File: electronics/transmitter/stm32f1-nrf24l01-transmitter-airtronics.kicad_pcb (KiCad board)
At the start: 2 copper layers, 107 x 36 mm, 31 parts, among them K1 CONN_3, K10 CONN_3, K11 CONN_3, K12 UART, K2 CONN_3, K3 CONN_3, K4 CONN_3, K5 CONN_3, K6 CONN_3, K7 CONN_3, K8 CONN_3, K9 CONN_3, P1 Charge, P2 LED, P3 PWR-BAT, P4 PWR-IN, P5 Buzzer, Q1 BC547B, SW1 ON/OFF, U1 LIPO_CHARGER_+_PROTECTION, U2 STM32F103C8T6_DEV_BOARD, U3 NRF24L01P

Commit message: Tweak layout
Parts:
- removed SP1: SPEAKER, WLA:Buzzer_passive
- added P1: Charge, Pin_Headers:Pin_Header_Straight_1x02_Pitch2.54mm, F.Cu at (276.9, 111.8)
- added REF**: MountingHole_3.2mm_M3, Mounting_Holes:MountingHole_3.2mm_M3, F.Cu at (210.8, 111.8)
- moved K12 15.2 mm to (241.3, 160.0)
- moved K10 13.7 mm to (221.0, 88.9)
- moved K8 13.7 mm to (228.6, 88.9)
- moved K11 13.7 mm to (223.5, 88.9)
- moved K9 13.7 mm to (226.1, 88.9)
- moved P3 12.7 mm to (276.9, 157.5)
- moved P4 12.7 mm to (269.2, 157.5)
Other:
- board size 107 x 36 mm -> 91.4 x 33 mm
- board text added: "+5V in charge/Red LED"
- board text added: "+After switch/+Buzzer"
- board text added: "+Batt protected"
- board text added: "-Red LED"
- board text added: "CH3"
- board text added: "DR-pot"
- board text added: "DR-switch"
- board text added: "ST"
- board text added: "ST-trim"
- board text added: "TH"
- board text added: "TH-trim"
- board text removed: "+5V in charge"
- board text removed: "+Switched/Buzzer"
- board text removed: "+batt protected"
- board text removed: "40"

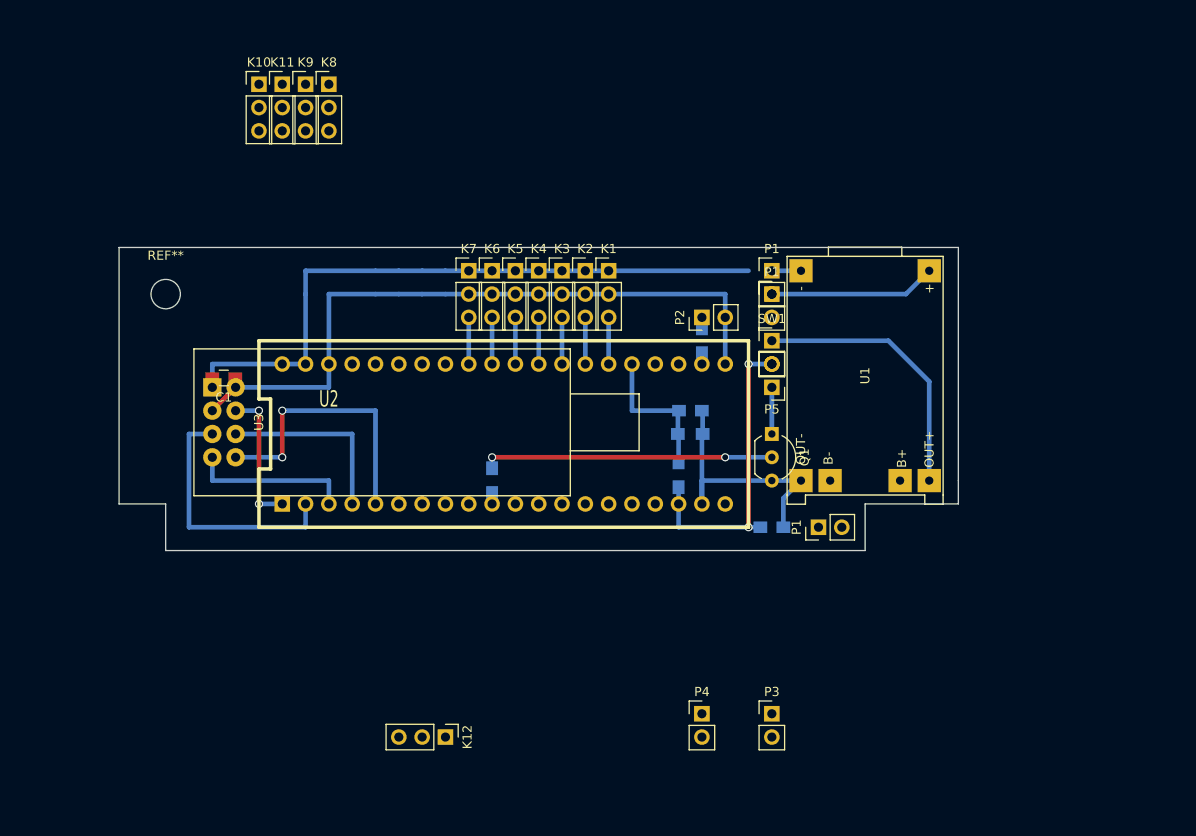
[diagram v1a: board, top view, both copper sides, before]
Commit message: Make PCB smaller and annotate
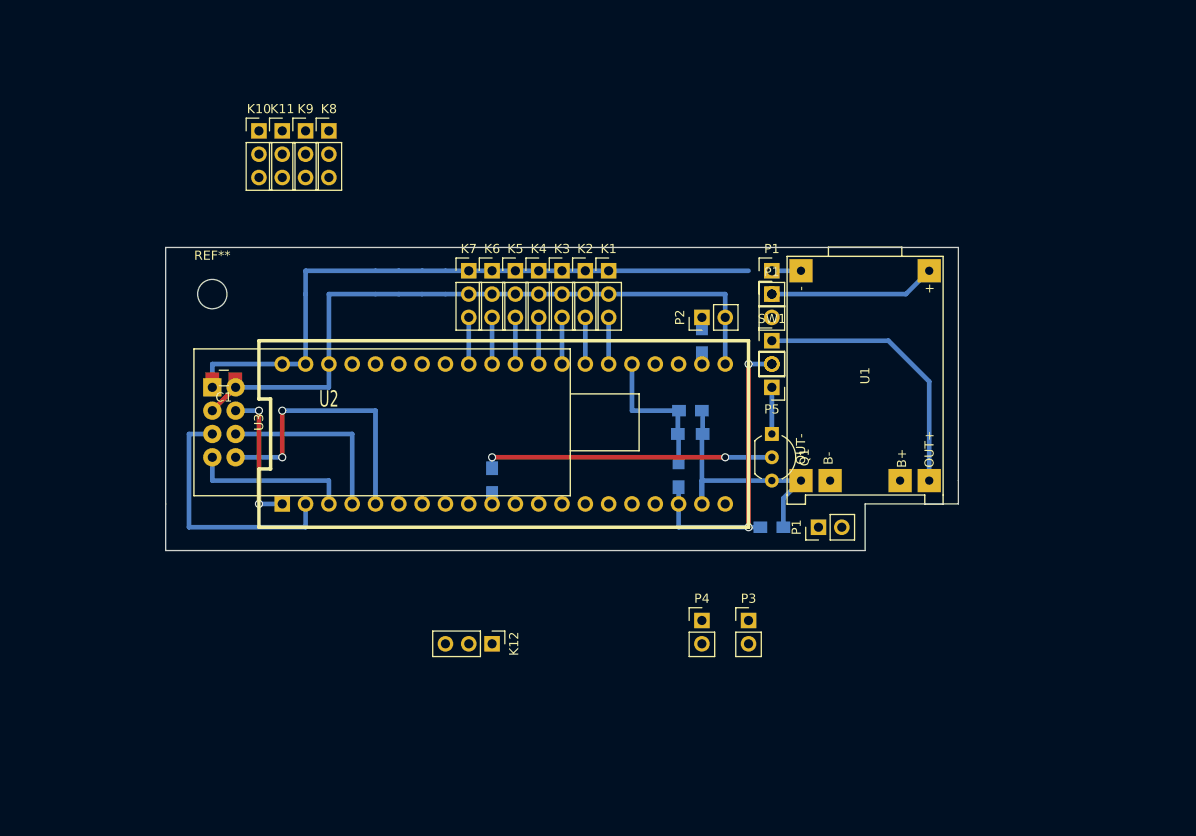
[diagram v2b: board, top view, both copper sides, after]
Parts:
- moved K12 11.4 mm to (246.4, 149.9)
- moved P3 10.5 mm to (274.3, 147.3)
- moved P4 10.2 mm to (269.2, 147.3)
- moved REF** 5.08 mm to (215.9, 111.8)
- moved K10 5.08 mm to (221.0, 94.0)
- moved K11 5.08 mm to (223.5, 94.0)
- moved K8 5.08 mm to (228.6, 94.0)
- moved K9 5.08 mm to (226.1, 94.0)
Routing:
- net Net-(P1-Pad2): track 18.8 -> 4.23 mm
- net Net-(P1-Pad1): track 3.18 -> 17.8 mm
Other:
- board size 91.4 x 33 mm -> 86.4 x 33 mm
- board text added: "34"
- board text added: "Links: 4, 2, 10, 7"
- board text removed: "35"

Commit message: Add annotations
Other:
- board text added: "This is not a PCB, but meant to be build on a prototyping PCB. It fits in the battery area of the Airtronics car transmitter. Modifications needed: STM32: remove BOOT pin header and tie to ground STM32: change programming pin header to vertical style TP4056: Change charge resistor to 2k7 (440mA) TP4056: Remove tabs near batt pads TP4056: Remove red LED, connect to pin header "-Red LED" nRF24L01+ 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"
- board text added: "Wire links needed: 4, 2, 10, 7"
- board text removed: "Links: 4, 2, 10, 7"
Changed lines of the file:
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@@
     (links 78)
     (no_connects 29)
-    (area 206.441257 89.742856 332.228571 153.2266)
+    (area 206.441257 89.742856 387.919999 165.235)
     (thickness 1.6)
-    (drawings 50)
+    (drawings 51)
     (tracks 102)
     (zones 0)
@@
     (41 Cmts.User user)
     (42 Eco1.User user hide)
-    (43 Eco2.User user hide)
+    (43 Eco2.User user)
     (44 Edge.Cuts user)
   )
@@
     (aux_axis_origin 210.82 139.7)
     (grid_origin 210.82 139.7)
-    (visible_elements 7FFCD71F)
+    (visible_elements 7FFCCF1F)
     (pcbplotparams
       (layerselection 0x00030_80000001)
@@
     (pad 1 np_thru_hole circle (at 0 0) (size 3.2 3.2) (drill 3.2) (layers *.Cu *.Mask))
   )
-  (gr_text "Links: 4, 2, 10, 7" (at 220.98 149.86) (layer Cmts.User)
-    (effects (font (size 2.032 2.032) (thickness 0.3)))
+  (gr_text "This is not a PCB, but meant to be build on a prototyping PCB.\nIt fits in the battery area of the Airtronics car transmitter.\n\nModifications needed:\nSTM32: remove BOOT pin header and tie to ground\nSTM32: change programming pin header to vertical style\nTP4056: Change charge resistor to 2k7 (440mA)\nTP4056: Remove tabs near batt pads\nTP4056: Remove red LED, connect to pin header \"-Red LED\"\nnRF24L01+ PA: Remove antenna socket and use antenna on wire\nnRF24L01+ PA: Longer pin headers\nnRF24L01+ PA: Connect CE to Vcc\nnRF24L01+ PA: Large cap between Vcc and GND" (at 312.42 149.86) (layer Eco2.User)
+    (effects (font (size 1.5 1.5) (thickness 0.3)) (justify left))
+  )
+  (gr_text "Wire links needed: 4, 2, 10, 7" (at 228.6 157.48) (layer Eco2.User)
+    (effects (font (thickness 0.3)))
   )
   (gr_line (start 210.82 106.68) (end 297.18 106.68) (angle 90) (layer Edge.Cuts) (width 0.1))
   (gr_line (start 210.82 134.62) (end 210.82 106.68) (angle 90) (layer Edge.Cuts) (width 0.1))
-  (gr_text DR-switch (at 243.84 101.6 90) (layer Cmts.User)
-    (effects (font (size 1.5 1.5) (thickness 0.3)) (justify left))
-  )
-  (gr_text DR-pot (at 246.38 101.6 90) (layer Cmts.User)
-    (effects (font (size 1.5 1.5) (thickness 0.3)) (justify left))
-  )
-  (gr_text TH (at 248.92 101.6 90) (layer Cmts.User)
-    (effects (font (size 1.5 1.5) (thickness 0.3)) (justify left))
-  )
-  (gr_text TH-trim (at 251.46 101.6 90) (layer Cmts.User)
-    (effects (font (size 1.5 1.5) (thickness 0.3)) (justify left))
-  )
-  (gr_text CH3 (at 254 101.6 90) (layer Cmts.User)
-    (effects (font (size 1.5 1.5) (thickness 0.3)) (justify left))
-  )
-  (gr_text ST-trim (at 256.54 101.6 90) (layer Cmts.User)
-    (effects (font (size 1.5 1.5) (thickness 0.3)) (justify left))
-  )
-  (gr_text ST (at 259.08 101.6 90) (layer Cmts.User)
+  (gr_text DR-switch (at 243.84 101.6 90) (layer Eco2.User)
+    (effects (font (size 1.5 1.5) (thickness 0.3)) (justify left))
+  )
+  (gr_text DR-pot (at 246.38 101.6 90) (layer Eco2.User)
+    (effects (font (size 1.5 1.5) (thickness 0.3)) (justify left))
+  )
+  (gr_text TH (at 248.92 101.6 90) (layer Eco2.User)
+    (effects (font (size 1.5 1.5) (thickness 0.3)) (justify left))
+  )
+  (gr_text TH-trim (at 251.46 101.6 90) (layer Eco2.User)
+    (effects (font (size 1.5 1.5) (thickness 0.3)) (justify left))
+  )
+  (gr_text CH3 (at 254 101.6 90) (layer Eco2.User)
+    (effects (font (size 1.5 1.5) (thickness 0.3)) (justify left))
+  )
+  (gr_text ST-trim (at 256.54 101.6 90) (layer Eco2.User)
+    (effects (font (size 1.5 1.5) (thickness 0.3)) (justify left))
+  )
+  (gr_text ST (at 259.08 101.6 90) (layer Eco2.User)
     (effects (font (size 1.5 1.5) (thickness 0.3)) (justify left))
   )
@@
   (gr_line (start 297.18 106.68) (end 297.18 132.08) (angle 90) (layer Edge.Cuts) (width 0.1))
   (gr_line (start 210.82 139.7) (end 210.82 134.62) (angle 90) (layer Edge.Cuts) (width 0.1))
-  (gr_text "-Red LED" (at 304.8 114.3) (layer Cmts.User)
-    (effects (font (size 1.5 1.5) (thickness 0.3)) (justify left))
-  )
-  (gr_text Meter- (at 269.24 101.6 90) (layer Cmts.User)
-    (effects (font (size 1.5 1.5) (thickness 0.3)) (justify left))
-  )
-  (gr_text Meter+ (at 271.78 101.6 90) (layer Cmts.User)
-    (effects (font (size 1.5 1.5) (thickness 0.3)) (justify left))
-  )
-  (gr_text Batt+ (at 284.48 144.78 90) (layer Cmts.User)
+  (gr_text "-Red LED" (at 304.8 114.3) (layer Eco2.User)
+    (effects (font (size 1.5 1.5) (thickness 0.3)) (justify left))
+  )
+  (gr_text Meter- (at 269.24 101.6 90) (layer Eco2.User)
+    (effects (font (size 1.5 1.5) (thickness 0.3)) (justify left))
+  )
+  (gr_text Meter+ (at 271.78 101.6 90) (layer Eco2.User)
+    (effects (font (size 1.5 1.5) (thickness 0.3)) (justify left))
+  )
+  (gr_text Batt+ (at 284.48 144.78 90) (layer Eco2.User)
     (effects (font (size 1.5 1.5) (thickness 0.3)) (justify right))
   )
-  (gr_text Batt- (at 281.94 144.78 90) (layer Cmts.User)
+  (gr_text Batt- (at 281.94 144.78 90) (layer Eco2.User)
     (effects (font (size 1.5 1.5) (thickness 0.3)) (justify right))
   )
-  (gr_text GND (at 304.8 109.22) (layer Cmts.User)
-    (effects (font (size 1.5 1.5) (thickness 0.3)) (justify left))
-  )
-  (gr_text "+5V in charge/Red LED" (at 304.8 111.76) (layer Cmts.User)
-    (effects (font (size 1.5 1.5) (thickness 0.3)) (justify left))
-  )
-  (gr_text "+Batt protected" (at 304.8 116.84) (layer Cmts.User)
-    (effects (font (size 1.5 1.5) (thickness 0.3)) (justify left))
-  )
-  (gr_text "+After switch/+Buzzer" (at 304.8 119.38) (layer Cmts.User)
-    (effects (font (size 1.5 1.5) (thickness 0.3)) (justify left))
-  )
-  (gr_text -Buzzer (at 304.8 121.92) (layer Cmts.User)
-    (effects (font (size 1.5 1.5) (thickness 0.3)) (justify left))
-  )
+  (gr_text GND (at 304.8 109.22) (layer Eco2.User)
+    (effects (font (size 1.5 1.5) (thickness 0.3)) (justify left))
+  )
+  (gr_text "+5V in charge/Red LED" (at 304.8 111.76) (layer Eco2.User)
+    (effects (font (size 1.5 1.5) (thickness 0.3)) (justify left))
+  )
+  (gr_text "+Batt protected" (at 304.8 116.84) (layer Eco2.User)
+    (effects (font (size 1.5 1.5) (thickness 0.3)) (justify left))
+  )
+  (gr_text "+After switch/+Buzzer" (at 304.8 119.38) (layer Eco2.User)
+    (effects (font (size 1.5 1.5) (thickness 0.3)) (justify left))
+  )
+  (gr_text -Buzzer (at 304.8 121.92) (layer Eco2.User)
+    (effects (font (size 1.5 1.5) (thickness 0.3)) (justify left))
+  )

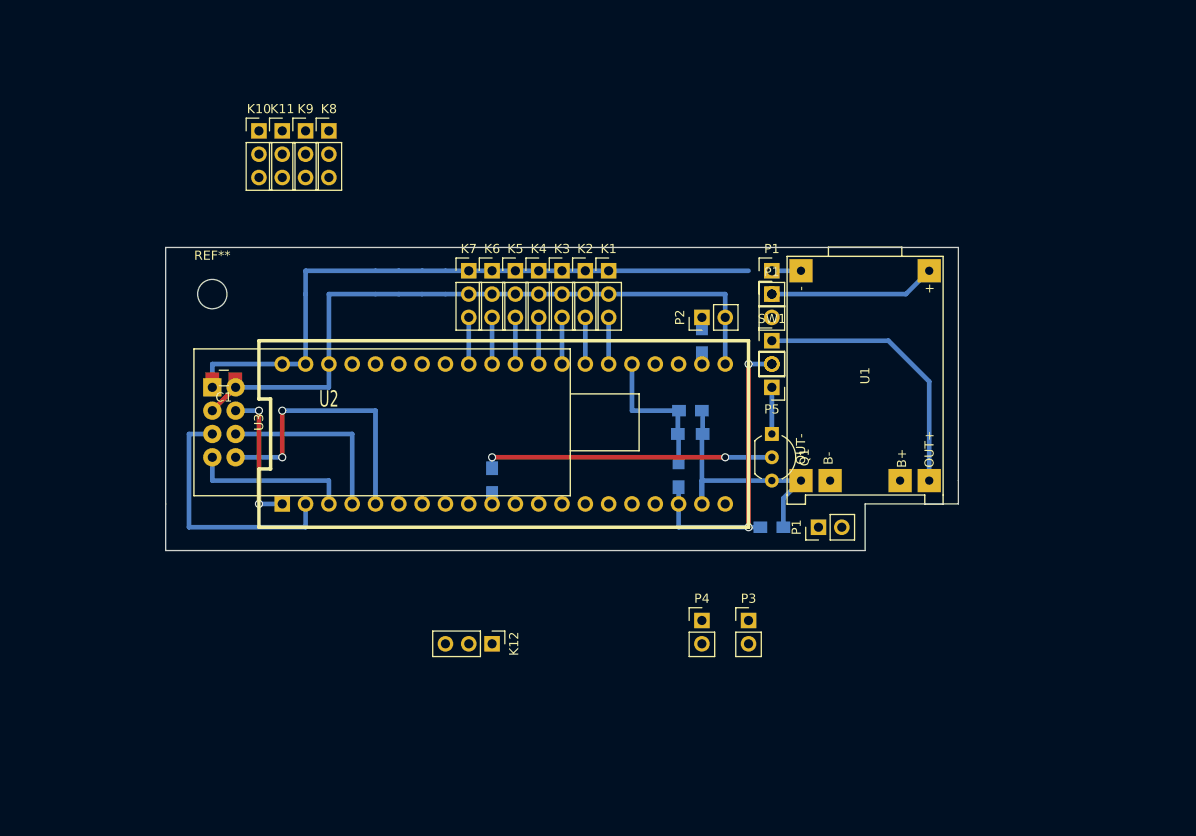
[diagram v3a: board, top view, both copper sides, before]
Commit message: Add analog meter output to electronics
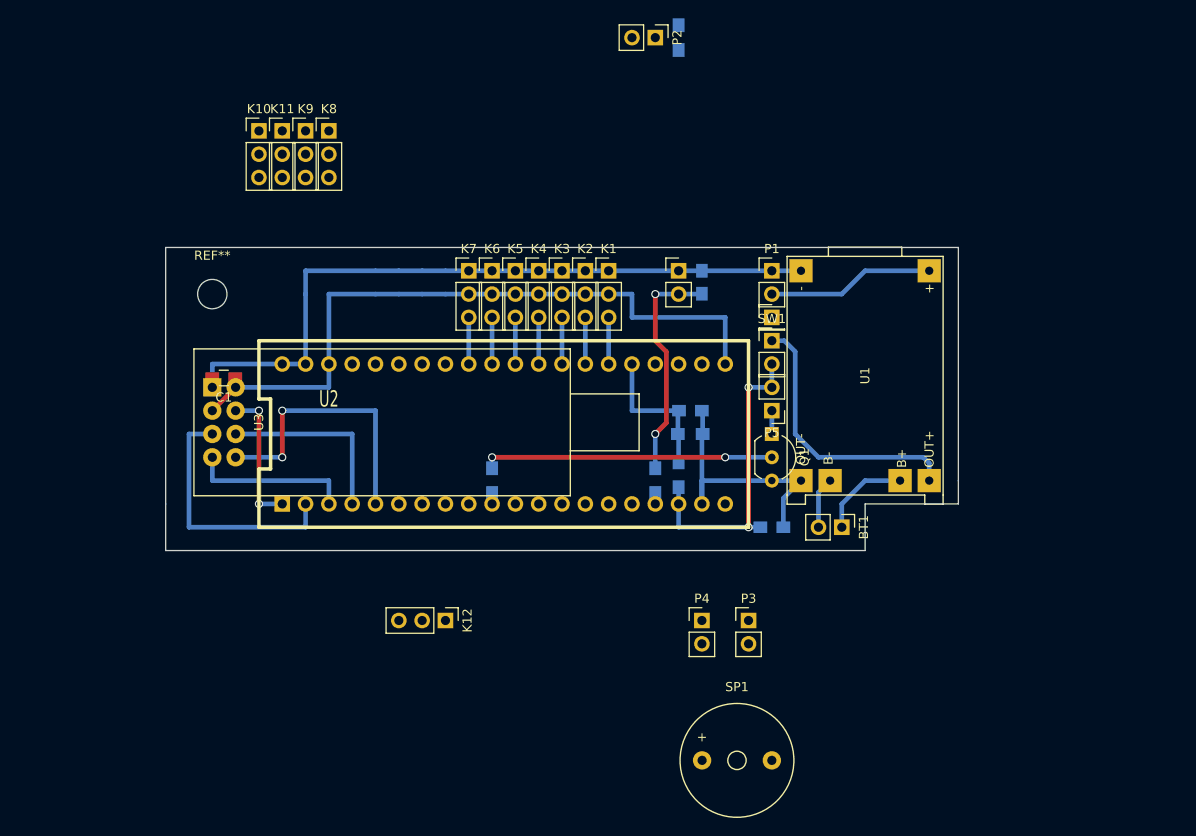
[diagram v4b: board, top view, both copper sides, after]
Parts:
- removed the P1 at (276.9, 111.8)
- removed the P1 at (281.9, 137.2)
- added BT1: BATTERY, Pin_Headers:Pin_Header_Straight_1x02_Pitch2.54mm, F.Cu at (284.5, 137.2)
- added C4: 1u, Capacitors_SMD:C_0805_HandSoldering, B.Cu at (269.2, 110.5)
- added P6: Meter, Pin_Headers:Pin_Header_Straight_1x02_Pitch2.54mm, F.Cu at (266.7, 109.2)
- added R5: 1k, Resistors_SMD:R_0805_HandSoldering, B.Cu at (264.2, 132.1)
- added REF**: Pin_Header_Straight_1x01_Pitch2.54mm, Pin_Headers:Pin_Header_Straight_1x01_Pitch2.54mm, F.Cu at (276.9, 114.3)
- added SP1: SPEAKER, Buzzers_Beepers:Buzzer_12x9.5RM7.6, F.Cu at (273.1, 162.6)
- moved R1 33.1 mm to (266.7, 83.8)
- moved P2 30.9 mm to (264.2, 83.8), turned to 270 degrees
- moved K12 5.68 mm to (241.3, 147.3)
- moved P5 2.54 mm to (276.9, 124.5)
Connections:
- P1 pad 1: Net-(P1-Pad1) -> GND
- U1 pad 6: Net-(P1-Pad1) -> GND
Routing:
- net Net-(C4-Pad1): track 0.00 -> 25.1 mm, vias 0 -> 2
- net Net-(P1-Pad1): track 17.8 -> 0.00 mm
- net Net-(P1-Pad2): track 4.23 -> 18.8 mm
- net Net-(BT1-Pad1): track 0.00 -> 9.94 mm
- net GND: track 100.6 -> 106.3 mm
- net Net-(BT1-Pad2): track 0.00 -> 5.61 mm
- net Net-(P5-Pad1): track 5.08 -> 2.54 mm
- net Net-(P2-Pad1): track 1.19 -> 0.00 mm
- net /PB9: track 0.00 -> 1.19 mm
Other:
- board text added: "+Buzzer"
- board text added: "SW"
- board text added: "This is not a PCB, but meant to be build on a prototyping board. It fits in the battery area of the Airtronics car transmitter. Modifications needed: STM32: remove BOOT pin header and tie to ground STM32: change programming pin header to vertical style STM32: only add pin headers where needed (e.g. NOT Pin24) TP4056: Change charge resistor to 2k7 (440mA) TP4056: Remove tabs near batt pads TP4056: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"
- board text added: "Wire links needed: 4, 2, 10, 6, 6"
- board text removed: "+After switch/+Buzzer"
- board text removed: "+Batt protected"
- board text removed: "This is not a PCB, but meant to be build on a prototyping PCB. It fits in the battery area of the Airtronics car transmitter. Modifications needed: STM32: remove BOOT pin header and tie to ground STM32: change programming pin header to vertical style TP4056: Change charge resistor to 2k7 (440mA) TP4056: Remove tabs near batt pads TP4056: Remove red LED, connect to pin header "-Red LED" nRF24L01+ 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"
- board text removed: "Wire links needed: 4, 2, 10, 7"
